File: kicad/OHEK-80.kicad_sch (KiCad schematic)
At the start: 231 parts, among them J1 USB_C_Receptacle_USB2.0_16P, J2 Conn_01x04, J3 Conn_01x05, SW1 SW_Push, SW2 SW_Push, U1 AMS1117-3.3, U10 GH39FKSW, U11 GH39FKSW, U12 GH39FKSW, U13 GH39FKSW, U14 GH39FKSW, U15 GH39FKSW, U16 GH39FKSW, U17 GH39FKSW, U18 GH39FKSW, U19 GH39FKSW, U2 RP2040, U20 GH39FKSW, U21 GH39FKSW, U22 GH39FKSW, U23 GH39FKSW, U24 GH39FKSW, U25 GH39FKSW, U26 GH39FKSW, U27 GH39FKSW, U28 GH39FKSW, U29 GH39FKSW, U3 GH39FKSW, U30 GH39FKSW, U31 GH39FKSW, U32 GH39FKSW, U33 GH39FKSW, U34 GH39FKSW, U35 GH39FKSW, U36 GH39FKSW, U37 GH39FKSW, U38 GH39FKSW, U39 GH39FKSW, U4 GH39FKSW, U40 GH39FKSW, U41 GH39FKSW, U42 GH39FKSW, U43 GH39FKSW, U44 GH39FKSW, U45 GH39FKSW, U46 GH39FKSW, U47 GH39FKSW, U48 GH39FKSW, U49 GH39FKSW, U5 GH39FKSW, U50 GH39FKSW, U51 GH39FKSW, U52 GH39FKSW, U53 GH39FKSW, U54 GH39FKSW, U55 GH39FKSW, U56 GH39FKSW, U57 GH39FKSW, U58 GH39FKSW, U59 GH39FKSW, U6 GH39FKSW, U60 GH39FKSW, U61 GH39FKSW, U62 GH39FKSW, U63 GH39FKSW, U64 GH39FKSW, U65 GH39FKSW, U66 GH39FKSW, U67 GH39FKSW, U68 GH39FKSW, U69 GH39FKSW, U7 GH39FKSW, U70 GH39FKSW, U71 GH39FKSW, U72 GH39FKSW, U73 GH39FKSW, U74 GH39FKSW, U75 GH39FKSW, U76 GH39FKSW, U77 GH39FKSW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

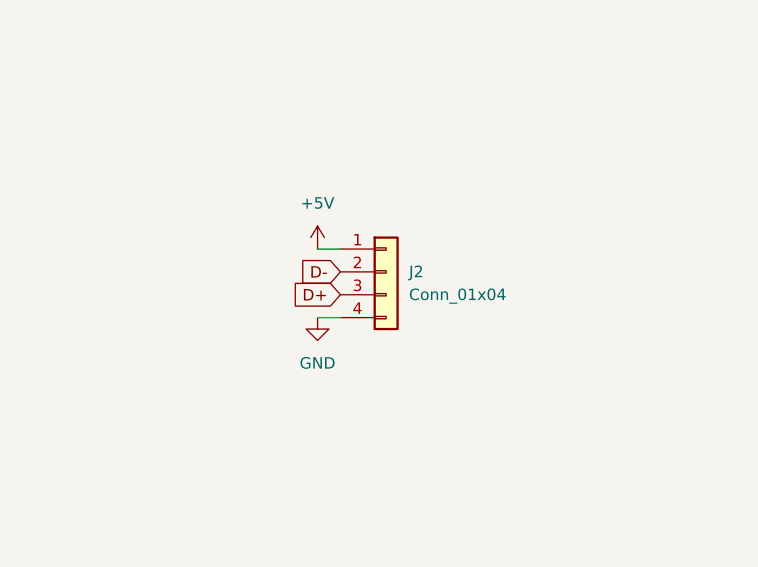
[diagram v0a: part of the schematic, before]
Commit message: Removed J2 and cleaned up PCB a bit
I realized that daughterboard support is useless as Void Switches are entirely contactless so there is no use in gasket mounting the keyboard.
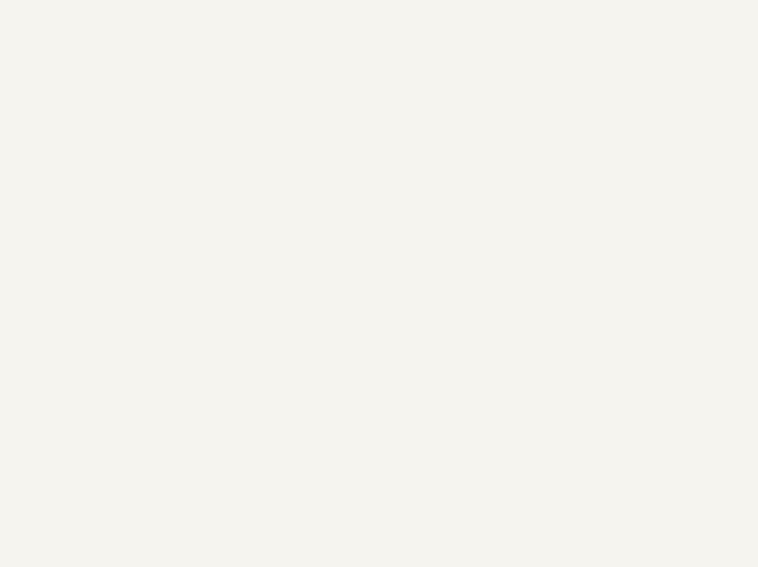
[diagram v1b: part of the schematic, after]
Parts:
- removed J2: Conn_01x04, Connector_JST:JST_PH_S4B-PH-K_1x04_P2.00mm_Horizontal, symbol Connector_Generic:Conn_01x04

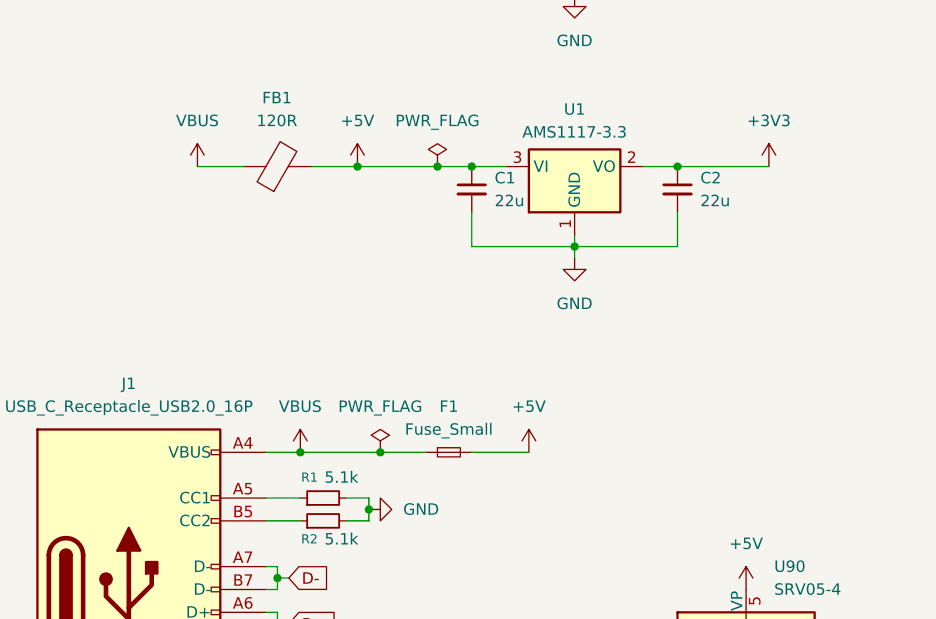
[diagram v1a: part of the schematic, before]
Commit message: Fix issue where FB1 and F1 were in parallel
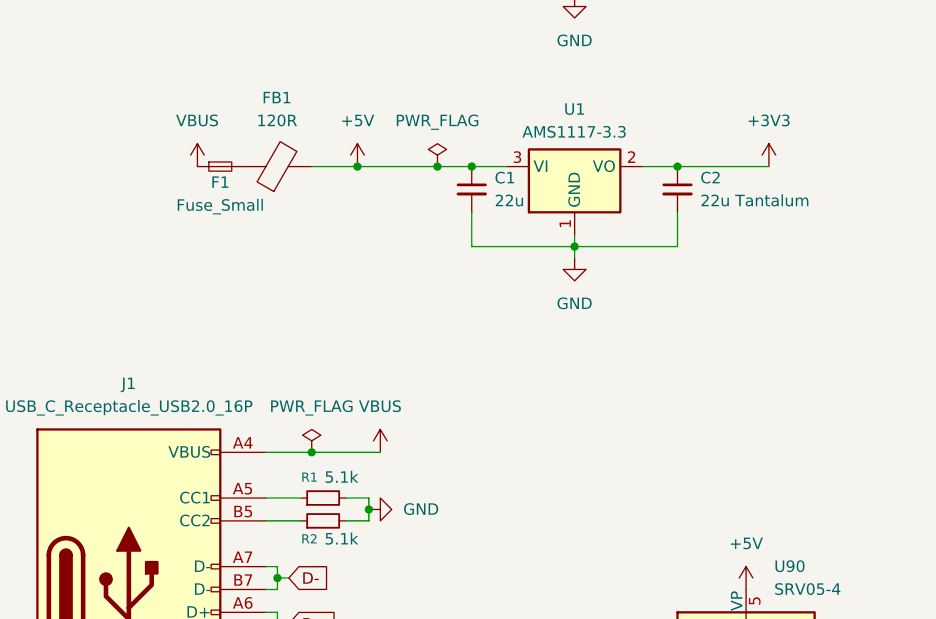
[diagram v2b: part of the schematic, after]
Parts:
- AM0, AM1, AM2, AM3, AM4, AM5, AMM1: LCSC (none) -> C98457
- C2: value 22u -> 22u Tantalum
- F1: LCSC (none) -> C13875
- FB1, FB2: LCSC C76892 -> C63224
- J1: LCSC (none) -> C165948
- J3: LCSC (none) -> C146054
- SW1, SW2: LCSC (none) -> C318884
- U1: LCSC (none) -> C6186
- U10, U11, U12, U13, U14, U15, U16, U17, U18, U19, U20, U21, U22, U23, U24, U25, U26, U27, U28, U29, U3, U30, U31, U32, U33, U34, U35, U36, U37, U38, U39, U4, U40, U41, U42, U43, U44, U45, U46, U47, U48, U49, U5, U50, U51, U52, U53, U54, U55, U56, U57, U58, U59, U6, U60, U61, U62, U63, U64, U65, U66, U67, U68, U69, U7, U70, U71, U72, U73, U74, U75, U76, U77, U78, U79, U8, U80, U81, U82, U83, U84, U85, U86, U87, U88, U89, U9: LCSC (none) -> C266230
- U2: LCSC (none) -> C2040
- U90: LCSC (none) -> C13612
- U91: LCSC (none) -> C97521
- Y1: LCSC (none) -> C20625731
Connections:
- net +5V: no longer F1.2
- net VBUS: no longer FB1.1
- new net: F1.2, FB1.1
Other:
- moved on the sheet: F1

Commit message: Fix incorrect footprints for SW1 and SW2
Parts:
- C2: LCSC (none) -> C1954754
- F1: LCSC C13875 -> C49318386
- FB1, FB2: LCSC C63224 -> C79382
- J3: LCSC C146054 -> C157923
- SW1, SW2: footprint Button_Switch_SMD:SW_SPST_PTS645Sx43SMTR92 -> Button_Switch_SMD:SW_SPST_TL3342
- U90: LCSC C13612 -> C7420376
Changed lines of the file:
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@@
 			)
 		)
-		(property "LCSC" "C63224"
+		(property "LCSC" "C79382"
 			(at 657.86 119.38 90)
 			(effects
@@
 			)
 		)
-		(property "LCSC" "C146054"
+		(property "LCSC" "C157923"
 			(at 508 179.07 0)
 			(effects
@@
 			)
 		)
-		(property "Footprint" "Button_Switch_SMD:SW_SPST_PTS645Sx43SMTR92"
+		(property "Footprint" "Button_Switch_SMD:SW_SPST_TL3342"
 			(at 500.38 215.9 0)
 			(effects
@@
 			)
 		)
-		(property "LCSC" "C13875"
+		(property "LCSC" "C49318386"
 			(at 651.51 119.38 0)
 			(effects
@@
 			)
 		)
-		(property "LCSC" "C63224"
+		(property "LCSC" "C79382"
 			(at 565.15 120.65 90)
 			(effects
@@
 			)
 		)
-		(property "LCSC" "C13612"
+		(property "LCSC" "C7420376"
 			(at 709.93 179.07 0)
 			(effects
@@
 			)
 		)
-		(property "Footprint" "Button_Switch_SMD:SW_SPST_PTS645Sx43SMTR92"
+		(property "Footprint" "Button_Switch_SMD:SW_SPST_TL3342"
 			(at 496.57 129.54 0)
 			(effects
@@
 			(at 702.31 121.92 0)
 			(effects
+				(font
+					(size 1.27 1.27)
+				)
+				(hide yes)
+			)
+		)
+		(property "LCSC" "C1954754"
+			(at 702.31 121.92 0)
+			(effects
